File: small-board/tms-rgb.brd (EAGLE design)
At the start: 54.4 x 17.6 mm, 39 parts, among them J1 Pads, U1 CD74HC4053PWR, U100 TMS992XA, U2 TS5A4597DCKR, U3 LM1881MX/NOPB, U4 MAX4395EUD, U5 SN74LVC2G17DCKR, U6 LMH1251MT/NOPB, U7 THS7374IPWR

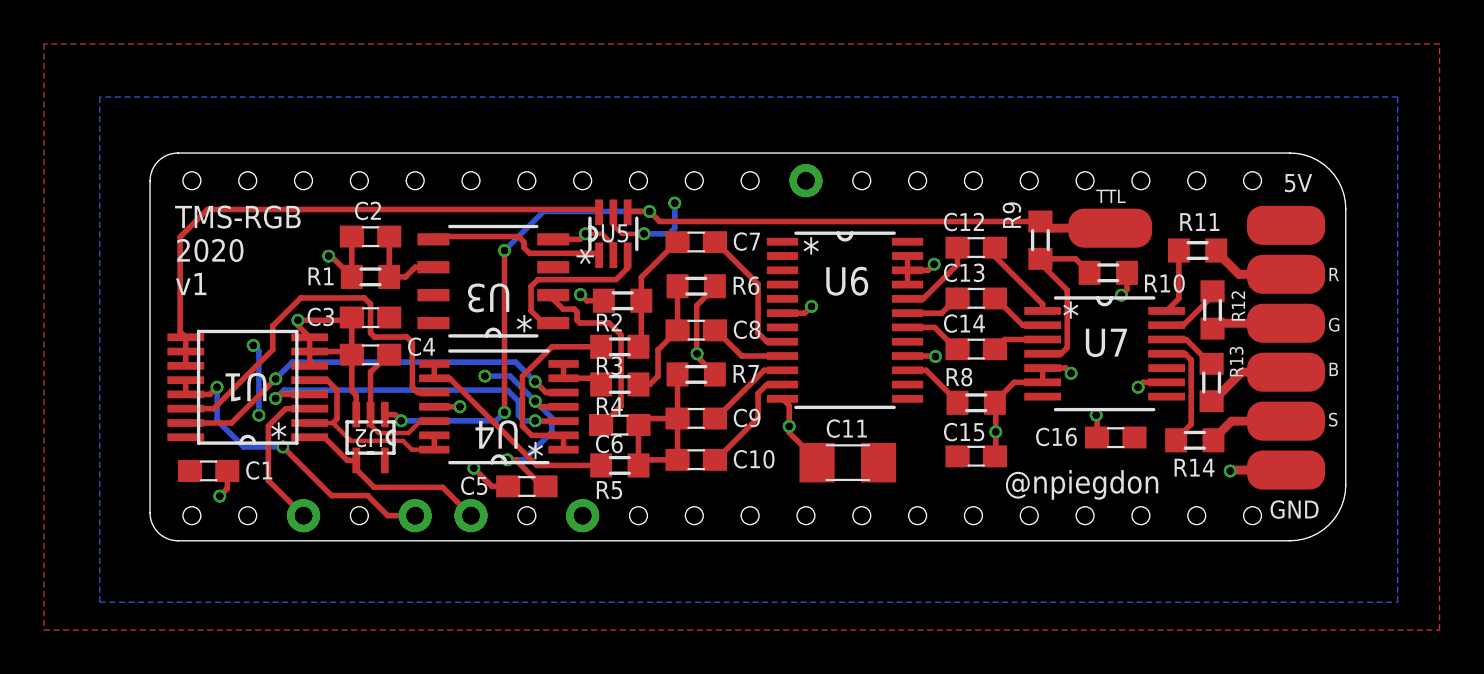
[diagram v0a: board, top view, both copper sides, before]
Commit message: Nudged C4 on the schematic
It's the sample-and-hold cap but its position (near the SPST instead of the op-amp) didn't reflect that clearly.
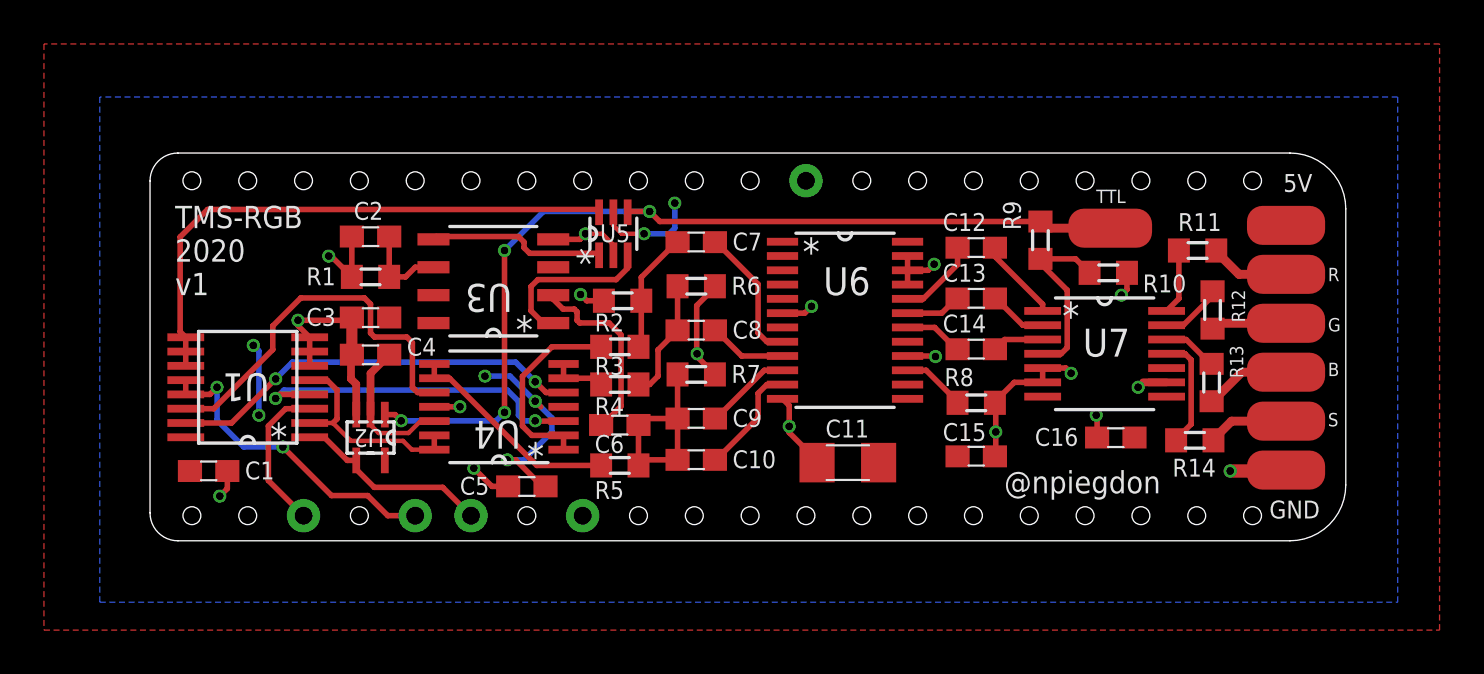
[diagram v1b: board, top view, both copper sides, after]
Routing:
- net GND: track 51.3 -> 49.3 mm
- net VCC: track 18.7 -> 17.7 mm
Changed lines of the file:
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@@
 <contactref element="C16" pad="2"/>
 <contactref element="C11" pad="2"/>
-<contactref element="C4" pad="2"/>
 <contactref element="C3" pad="2"/>
 <contactref element="J1" pad="6"/>
@@
 <wire x1="35.40458125" y1="12.308" x2="35.678290625" y2="12.581709375" width="0.254" layer="1"/>
 <via x="35.678290625" y="12.581709375" extent="1-16" drill="0.35"/>
-<wire x1="51.689" y1="3.217328125" x2="49.191328125" y2="3.217328125" width="0.4064" layer="1"/>
-<wire x1="49.191328125" y1="3.217328125" x2="49.149" y2="3.175" width="0.4064" layer="1"/>
-<via x="49.149" y="3.175" extent="1-16" drill="0.35"/>
+<via x="49.149" y="3.175" extent="1-16" drill="0.3556"/>
 <contactref element="C1" pad="2"/>
 <contactref element="C15" pad="2"/>
@@
 <wire x1="41.671" y1="7.859" x2="41.91" y2="7.62" width="0.254" layer="1"/>
 <via x="41.91" y="7.62" extent="1-16" drill="0.35"/>
-<wire x1="46.2534" y1="7.209" x2="45.182" y2="7.209" width="0.254" layer="1"/>
+<wire x1="46.2534" y1="7.209" x2="45.182" y2="7.209" width="0.3556" layer="1"/>
 <wire x1="45.182" y1="7.209" x2="44.958" y2="6.985" width="0.254" layer="1"/>
 <via x="44.958" y="6.985" extent="1-16" drill="0.35"/>
@@
 <wire x1="14.097" y1="6.096" x2="14.101840625" y2="6.100840625" width="0.254" layer="1"/>
 <via x="14.101840625" y="6.100840625" extent="1-16" drill="0.35"/>
-<wire x1="9.383" y1="5.7404" x2="9.383" y2="6.619" width="0.254" layer="1"/>
-<wire x1="9.183" y1="6.819" x2="9.183" y2="8.466665625" width="0.254" layer="1"/>
-<wire x1="9.383" y1="6.619" x2="9.183" y2="6.819" width="0.254" layer="1"/>
 <wire x1="9.183" y1="12.008553125" x2="9.183" y2="13.842996875" width="0.254" layer="1"/>
-<wire x1="9.183" y1="8.466665625" x2="9.03966875" y2="8.609996875" width="0.254" layer="1"/>
-<wire x1="9.03966875" y1="8.609996875" x2="7.2644" y2="8.609996875" width="0.254" layer="1"/>
-<wire x1="9.183" y1="8.466665625" x2="9.183" y2="10.16" width="0.254" layer="1"/>
 <wire x1="9.183" y1="12.008553125" x2="8.237553125" y2="12.954" width="0.254" layer="1"/>
 <wire x1="8.237553125" y1="12.954" x2="8.128" y2="12.954" width="0.254" layer="1"/>
@@
 <wire x1="21.082" y1="13.4633125" x2="21.082" y2="12.9921" width="0.2032" layer="1"/>
 <wire x1="19.812" y1="13.97" x2="20.5753125" y2="13.97" width="0.2032" layer="1"/>
+<wire x1="51.646671875" y1="3.175" x2="51.689" y2="3.217328125" width="0.6096" layer="1"/>
+<wire x1="49.149" y1="3.175" x2="51.646671875" y2="3.175" width="0.6096" layer="1"/>
+<contactref element="C4" pad="2"/>
+<wire x1="9.383" y1="5.7404" x2="9.383" y2="7.127" width="0.3556" layer="1"/>
+<wire x1="9.383" y1="7.127" x2="9.144" y2="7.366" width="0.3556" layer="1"/>
+<wire x1="9.144" y1="7.366" x2="9.144" y2="8.427665625" width="0.3556" layer="1"/>
+<wire x1="9.144" y1="8.427665625" x2="9.183" y2="8.466665625" width="0.3556" layer="1"/>
+<wire x1="9.183" y1="8.466665625" x2="9.183" y2="10.16" width="0.508" layer="1"/>
 </signal>
 <signal name="VCC">
@@
 <contactref element="U6" pad="24"/>
 <contactref element="U6" pad="7"/>
-<contactref element="U4" pad="4"/>
 <contactref element="U2" pad="5"/>
 <contactref element="C16" pad="1"/>
@@
 </polygon>
 <via x="17.526" y="6.35" extent="1-16" drill="0.35"/>
-<wire x1="18.81505" y1="6.096" x2="17.78" y2="6.096" width="0.254" layer="1"/>
 <wire x1="17.78" y1="6.096" x2="17.526" y2="6.35" width="0.254" layer="1"/>
 <contactref element="U5" pad="5"/>
@@
 <wire x1="21.082" y1="14.351" x2="21.463" y2="13.97" width="0.2032" layer="1"/>
 <wire x1="21.463" y1="13.97" x2="22.479" y2="13.97" width="0.2032" layer="1"/>
+<contactref element="U4" pad="4"/>
 </signal>
 <signal name="N$12">
@@
 <wire x1="49.547753125" y1="12.124240625" x2="51.689" y2="12.124240625" width="0.4064" layer="1"/>
 </signal>
-<signal name="N$35">
-<contactref element="U4" pad="12"/>
-<contactref element="U2" pad="2"/>
-<contactref element="C4" pad="1"/>
-<wire x1="12.93495" y1="5.446" x2="12.304" y2="5.446" width="0.2032" layer="1"/>
-<wire x1="10.3999875" y1="4.9022" x2="10.033" y2="5.2691875" width="0.2032" layer="1"/>
-<wire x1="10.033" y1="5.2691875" x2="10.033" y2="5.7404" width="0.2032" layer="1"/>
-<wire x1="12.304" y1="5.446" x2="11.7602" y2="4.9022" width="0.2032" layer="1"/>
-<wire x1="11.7602" y1="4.9022" x2="10.3999875" y2="4.9022" width="0.2032" layer="1"/>
-<wire x1="10.883" y1="8.466665625" x2="10.833" y2="8.466665625" width="0.254" layer="1"/>
-<wire x1="10.833" y1="8.466665625" x2="10.033" y2="7.666665625" width="0.254" layer="1"/>
-<wire x1="10.033" y1="7.666665625" x2="10.033" y2="5.7404" width="0.254" layer="1"/>
-</signal>
 <signal name="N$5">
 <contactref element="U3" pad="5"/>
@@
 <wire x1="1.6256" y1="7.96" x2="1.6256" y2="8.61" width="0.254" layer="1"/>
 </signal>
+<signal name="N$4">
+<contactref element="U4" pad="12"/>
+<contactref element="C4" pad="1"/>
+<contactref element="U2" pad="2"/>
+<wire x1="10.033" y1="7.616665625" x2="10.883" y2="8.466665625" width="0.3556" layer="1"/>
+<wire x1="10.033" y1="5.7404" x2="10.033" y2="7.616665625" width="0.3556" layer="1"/>
+<wire x1="12.93495" y1="5.446" x2="12.304" y2="5.446" width="0.2032" layer="1"/>
+<wire x1="10.3999875" y1="4.9022" x2="10.033" y2="5.2691875" width="0.2032" layer="1"/>
+<wire x1="10.033" y1="5.2691875" x2="10.033" y2="5.7404" width="0.2032" layer="1"/>
+<wire x1="12.304" y1="5.446" x2="11.7602" y2="4.9022" width="0.2032" layer="1"/>
+<wire x1="11.7602" y1="4.9022" x2="10.3999875" y2="4.9022" width="0.2032" layer="1"/>
+</signal>
 </signals>
